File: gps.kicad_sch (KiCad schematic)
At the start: 17 parts, among them J700 Conn_01x02, U700 NEO-6P, X7 Conn_Coaxial

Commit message: worked on bom. some changes. added license
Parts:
- C561, R700, R704, R705, R706: JLC_placed_by (none) -> yes
- J700, U700, X7: JLC_placed_by (none) -> no
- JP700, JP701, JP702, JP703, JP704, JP705, TP700, TP701: JLC_placed_by (none) -> never
- L700: JLC_placed_by (none) -> yes; JLCplace (none) -> C56586
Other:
- note added: "Do not place R704 if you use ublox NEO-9"
- note added: "NEO-6 / 7 / 8 / 9 are pin compatible und supported."
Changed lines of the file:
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@@
     (stroke (width 0) (type solid) (color 0 0 0 0))
+  )
+  (text "Do not place R704 if you use ublox NEO-9" (at 154.94 50.8 0)
+    (effects (font (size 1.27 1.27)) (justify left bottom))
+  )
+  (text "NEO-6 / 7 / 8 / 9 are pin compatible und supported. "
+    (at 154.94 121.92 0)
+    (effects (font (size 1.27 1.27)) (justify left bottom))
   )
   (global_label "TIME_MEAS" (shape input) (at 114.3 97.79 180)
@@
       (effects (font (size 1.27 1.27)) hide)
     )
+    (property "JLC_placed_by" "never" (id 5) (at 222.25 95.25 0)
+      (effects (font (size 1.27 1.27)) hide)
+    )
     (pin "1")
     (pin "2")
@@
     )
     (property "JLCplace" "C17477" (id 9) (at 154.94 59.69 0)
+      (effects (font (size 1.27 1.27)) hide)
+    )
+    (property "JLC_placed_by" "yes" (id 10) (at 154.94 59.69 0)
       (effects (font (size 1.27 1.27)) hide)
     )
@@
       (effects (font (size 1.27 1.27)) hide)
     )
+    (property "JLC_placed_by" "yes" (id 10) (at 170.18 66.04 0)
+      (effects (font (size 1.27 1.27)) hide)
+    )
     (pin "1")
     (pin "2")
@@
     )
     (property "JLCplace" "C49678" (id 9) (at 93.98 129.54 0)
+      (effects (font (size 1.27 1.27)) hide)
+    )
+    (property "JLC_placed_by" "yes" (id 10) (at 93.98 129.54 0)
       (effects (font (size 1.27 1.27)) hide)
     )
@@
     )
     (property "Supplier" "??" (id 4) (at 146.05 87.63 0)
+      (effects (font (size 1.27 1.27)) hide)
+    )
+    (property "JLC_placed_by" "no" (id 5) (at 146.05 87.63 0)
       (effects (font (size 1.27 1.27)) hide)
     )
@@
       (effects (font (size 1.27 1.27)) hide)
     )
+    (property "JLC_placed_by" "yes" (id 10) (at 208.28 85.09 0)
+      (effects (font (size 1.27 1.27)) hide)
+    )
     (pin "1")
     (pin "2")
@@
       (effects (font (size 1.27 1.27)) hide)
     )
+    (property "JLC_placed_by" "never" (id 5) (at 102.87 80.01 0)
+      (effects (font (size 1.27 1.27)) hide)
+    )
     (pin "1")
     (pin "2")
@@
     )
     (property "Supplier" "--" (id 4) (at 109.22 85.09 0)
+      (effects (font (size 1.27 1.27)) hide)
+    )
+    (property "JLC_placed_by" "never" (id 5) (at 109.22 85.09 0)
       (effects (font (size 1.27 1.27)) hide)
     )
@@
       (effects (font (size 1.27 1.27)) hide)
     )
+    (property "JLC_placed_by" "yes" (id 10) (at 208.28 95.25 0)
+      (effects (font (size 1.27 1.27)) hide)
+    )
     (pin "1")
     (pin "2")
@@
       (effects (font (size 1.27 1.27)) hide)
     )
+    (property "JLC_placed_by" "never" (id 5) (at 120.65 97.79 0)
+      (effects (font (size 1.27 1.27)) hide)
+    )
     (pin "1")
     (pin "2")
@@
       (effects (font (size 1.27 1.27)) hide)
     )
+    (property "JLC_placed_by" "never" (id 5) (at 102.87 82.55 0)
+      (effects (font (size 1.27 1.27)) hide)
+    )
     (pin "1")
     (pin "2")
@@
     )
     (property "alternativ supply part nr." "CE201210-27NJ" (id 10) (at 170.18 74.93 0)
+      (effects (font (size 1.27 1.27)) hide)
+    )
+    (property "JLC_placed_by" "yes" (id 11) (at 170.18 74.93 0)
+      (effects (font (size 1.27 1.27)) hide)
+    )
+    (property "JLCplace" "C56586" (id 12) (at 170.18 74.93 0)
       (effects (font (size 1.27 1.27)) hide)
     )
@@
       (effects (font (size 1.27 1.27)) hide)
     )
+    (property "JLC_placed_by" "never" (id 5) (at 123.19 87.63 0)
+      (effects (font (size 1.27 1.27)) hide)
+    )
     (pin "1")
     (pin "2")
@@
       (effects (font (size 1.27 1.27)) hide)
     )
+    (property "JLC_placed_by" "no" (id 6) (at 222.25 82.55 0)
+      (effects (font (size 1.27 1.27)) hide)
+    )
     (pin "1")
     (pin "2")
@@
       (effects (font (size 1.27 1.27)) hide)
     )
+    (property "JLC_placed_by" "no" (id 9) (at 176.53 80.01 0)
+      (effects (font (size 1.27 1.27)) hide)
+    )
     (pin "1")
     (pin "2")
@@
       (effects (font (size 1.27 1.27)) hide)
     )
+    (property "JLC_placed_by" "never" (id 5) (at 123.19 90.17 0)
+      (effects (font (size 1.27 1.27)) hide)
+    )
     (pin "1")
     (pin "2")
@@
       (effects (font (size 1.27 1.27)) hide)
     )
+    (property "JLC_placed_by" "never" (id 5) (at 109.22 77.47 0)
+      (effects (font (size 1.27 1.27)) hide)
+    )

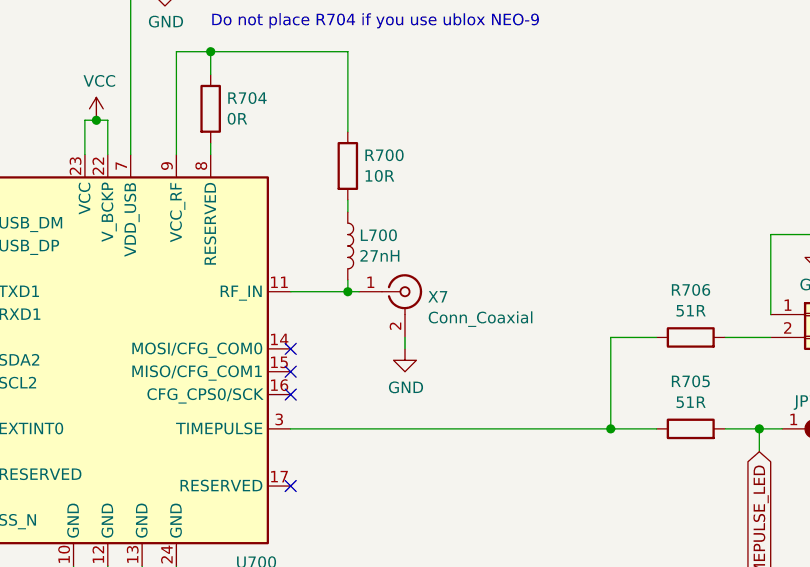
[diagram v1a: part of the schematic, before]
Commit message: Updated schematic and pcb to use global muonpi library
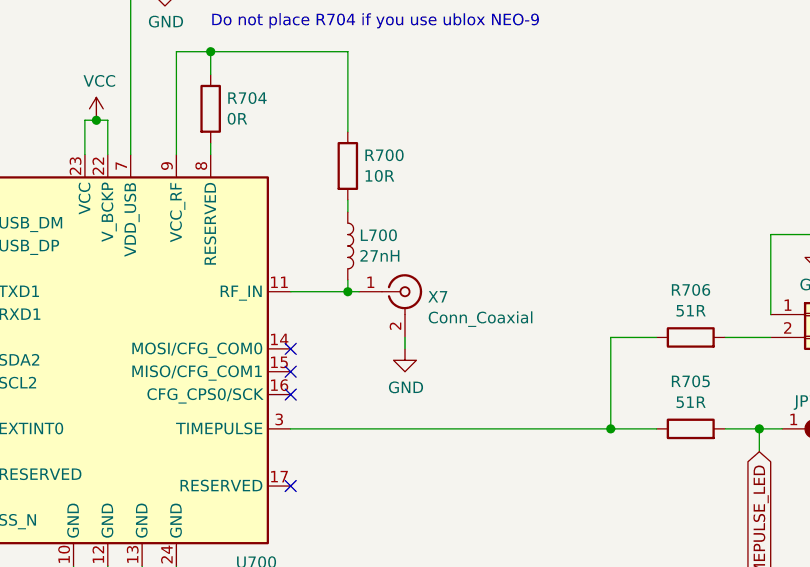
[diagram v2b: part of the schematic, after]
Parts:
- U700: footprint muonpi-kicad-library:ublox_NEO -> muonpi:ublox_NEO; symbol muonpi-kicad-library:NEO-6P -> muonpi:NEO-6P
- X7: footprint muonpi-kicad-library:Connector_Coaxial_SMA_edge_combined -> muonpi:SMA_Samtec_SMA-J-P-X-ST-EM1_EdgeMount; symbol muonpi-kicad-library:Conn_Coaxial -> muonpi:Conn_Coaxial
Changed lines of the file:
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@@
     (pin "2")
   )
-  (symbol (lib_id "muonpi-kicad-library:NEO-6P") (at 146.05 87.63 0) (unit 1)
+  (symbol (lib_id "muonpi:NEO-6P") (at 146.05 87.63 0) (unit 1)
     (in_bom yes) (on_board yes)
     (property "Reference" "U700" (id 0) (at 160.02 110.109 0))
     (property "Value" "NEO-6P" (id 1) (at 161.29 112.4141 0))
-    (property "Footprint" "muonpi-kicad-library:ublox_NEO" (id 2) (at 161.29 109.22 0)
+    (property "Footprint" "muonpi:ublox_NEO" (id 2) (at 161.29 109.22 0)
       (effects (font (size 1.27 1.27)) hide)
     )
@@
     (pin "1")
   )
-  (symbol (lib_id "muonpi-kicad-library:Conn_Coaxial") (at 176.53 80.01 0) (unit 1)
+  (symbol (lib_id "muonpi:Conn_Coaxial") (at 176.53 80.01 0) (unit 1)
     (in_bom yes) (on_board yes)
     (property "Reference" "X7" (id 0) (at 179.07 80.6196 0)
@@
       (effects (font (size 1.27 1.27)) (justify left))
     )
-    (property "Footprint" "muonpi-kicad-library:Connector_Coaxial_SMA_edge_combined" (id 2) (at 176.53 80.01 0)
-      (effects (font (size 1.27 1.27)) hide)
-    )
+    (property "Footprint" "muonpi:SMA_Samtec_SMA-J-P-X-ST-EM1_EdgeMount" (id 2) (at 176.53 80.01 0)
+      (effects (font (size 1.27 1.27)) hide)
+    )
